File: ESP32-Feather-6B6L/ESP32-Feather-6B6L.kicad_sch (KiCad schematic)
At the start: 1 part

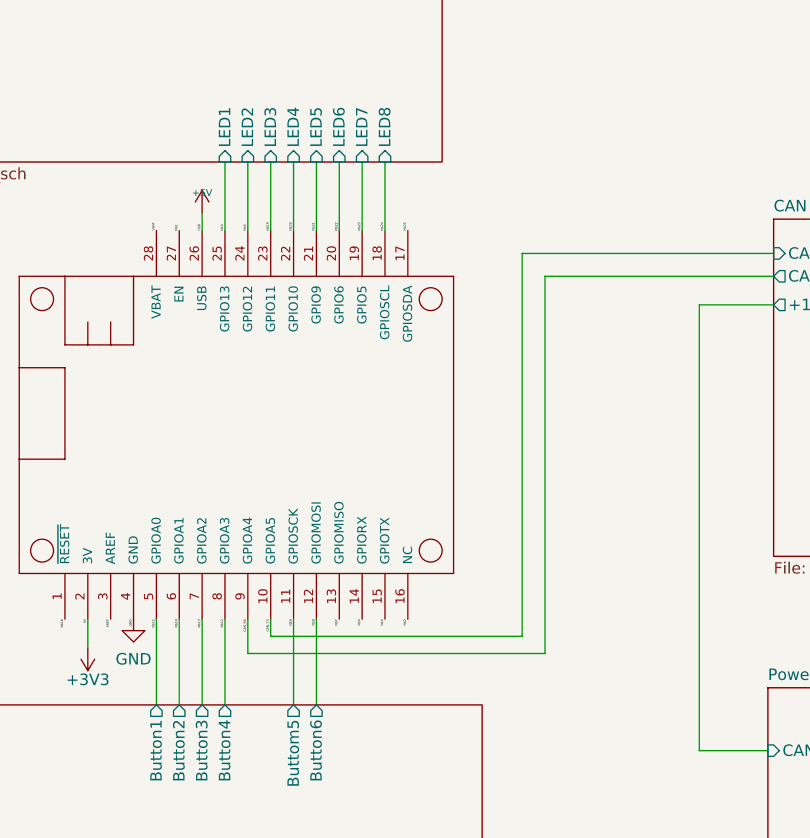
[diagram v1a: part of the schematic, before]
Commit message: Rescue SCL.
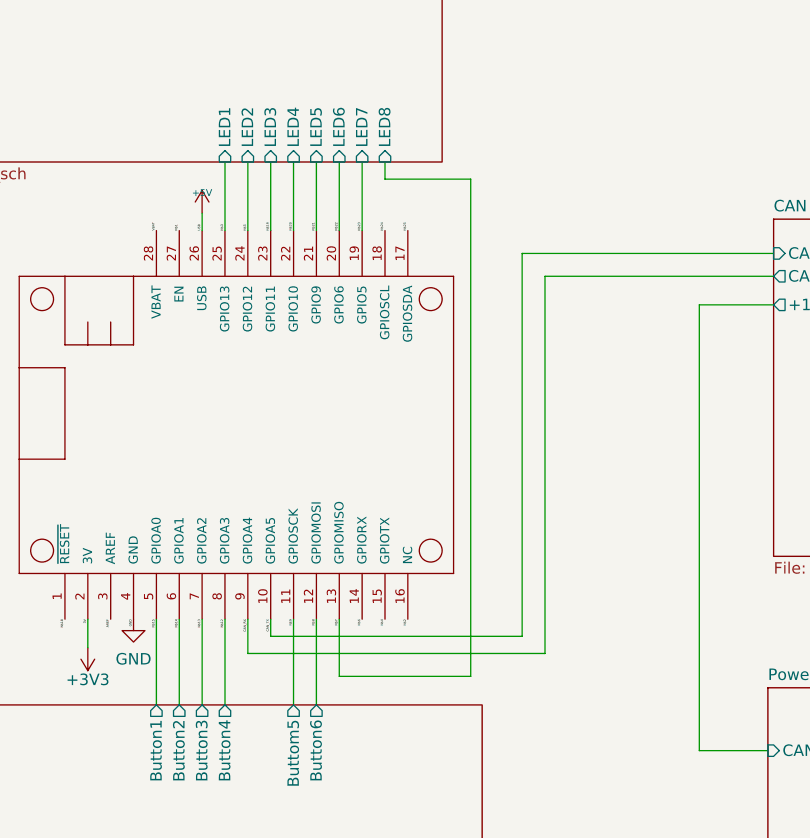
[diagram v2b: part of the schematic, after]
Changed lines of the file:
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@@
     (stroke (width 0) (type default) (color 0 0 0 0))
   )
-  (wire (pts (xy 125.095 59.055) (xy 125.095 66.675))
+  (wire (pts (xy 125.095 60.96) (xy 134.62 60.96))
     (stroke (width 0) (type default) (color 0 0 0 0))
   )
@@
     (stroke (width 0) (type default) (color 0 0 0 0))
   )
+  (wire (pts (xy 134.62 60.96) (xy 134.62 116.205))
+    (stroke (width 0) (type default) (color 0 0 0 0))
+  )
   (wire (pts (xy 160.02 74.93) (xy 160.02 124.46))
     (stroke (width 0) (type default) (color 0 0 0 0))
@@
   )
   (wire (pts (xy 104.775 109.855) (xy 104.775 119.38))
+    (stroke (width 0) (type default) (color 0 0 0 0))
+  )
+  (wire (pts (xy 125.095 59.055) (xy 125.095 60.96))
     (stroke (width 0) (type default) (color 0 0 0 0))
   )
@@
     (stroke (width 0) (type default) (color 0 0 0 0))
   )
+  (wire (pts (xy 134.62 116.205) (xy 120.015 116.205))
+    (stroke (width 0) (type default) (color 0 0 0 0))
+  )
   (wire (pts (xy 102.235 109.855) (xy 102.235 119.38))
     (stroke (width 0) (type default) (color 0 0 0 0))
@@
     (stroke (width 0) (type default) (color 0 0 0 0))
   )
+  (wire (pts (xy 120.015 109.855) (xy 120.015 116.205))
+    (stroke (width 0) (type default) (color 0 0 0 0))
+  )
